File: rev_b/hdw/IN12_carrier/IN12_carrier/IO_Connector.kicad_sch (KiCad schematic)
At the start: 0 parts

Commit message: lots of placement progress on IN12 carrier board
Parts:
- added J1901: Conn_02x32_Top_Bottom, Custom Footprints Library:CONN_5120528-1_TYC, symbol Connector_Generic:Conn_02x32_Top_Bottom
- added R?: 499, Resistors_SMD:R_0603, symbol Custom_Library:R_Custom
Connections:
- new net +180V: J1901.36 (Pin_36), J1901.37 (Pin_37)
- new net +3.3V: J1901.61 (Pin_61), J1901.62 (Pin_62), J1901.63 (Pin_63), J1901.64 (Pin_64)
- new net +90V: J1901.33 (Pin_33), J1901.34 (Pin_34)
- new net Anode_0_DSP: J1901.39 (Pin_39)
- new net Anode_1_DSP: J1901.7 (Pin_7)
- new net Anode_2_DSP: J1901.40 (Pin_40)
- new net Anode_3_DSP: J1901.8 (Pin_8)
- new net Anode_4_DSP: J1901.41 (Pin_41)
- new net Anode_5_DSP: J1901.9 (Pin_9)
- new net Cathode_0_DSP: J1901.43 (Pin_43)
- new net Cathode_1_DSP: J1901.11 (Pin_11)
- new net Cathode_2_DSP: J1901.44 (Pin_44)
- new net Cathode_3_DSP: J1901.12 (Pin_12)
- new net Cathode_4_DSP: J1901.45 (Pin_45)
- new net Cathode_5_DSP: J1901.13 (Pin_13)
- new net Cathode_6_DSP: J1901.46 (Pin_46)
- new net Cathode_7_DSP: J1901.14 (Pin_14)
- new net Cathode_8_DSP: J1901.47 (Pin_47)
- new net Cathode_9_DSP: J1901.15 (Pin_15)
- new net Cathode_DP_DSP: J1901.48 (Pin_48)
- new net Colon_0_DSP: J1901.50 (Pin_50)
- new net Colon_1_DSP: J1901.18 (Pin_18)
- new net Colon_2_DSP: J1901.51 (Pin_51)
- new net Colon_3_DSP: J1901.19 (Pin_19)
- new net GND: J1901.1 (Pin_1), J1901.10 (Pin_10), J1901.16 (Pin_16), J1901.17 (Pin_17), J1901.2 (Pin_2), J1901.20 (Pin_20), J1901.24 (Pin_24), J1901.25 (Pin_25), J1901.29 (Pin_29), J1901.3 (Pin_3), J1901.30 (Pin_30), J1901.31 (Pin_31), J1901.32 (Pin_32), J1901.4 (Pin_4), J1901.42 (Pin_42), J1901.49 (Pin_49), J1901.5 (Pin_5), J1901.52 (Pin_52), J1901.6 (Pin_6), R?.2
- new net I2C_DSP_SCL: J1901.58 (Pin_58)
- new net I2C_DSP_SDA: J1901.26 (Pin_26)
- new net Pushbutton_0_DSP: J1901.53 (Pin_53)
- new net Pushbutton_1_DSP: J1901.21 (Pin_21)
- new net Pushbutton_2_DSP: J1901.54 (Pin_54)
- new net Pushbutton_3_DSP: J1901.22 (Pin_22)
- new net Pushbutton_4_DSP: J1901.55 (Pin_55)
- new net Pushbutton_5_DSP: J1901.23 (Pin_23)
- new net Pushbutton_6_DSP: J1901.56 (Pin_56)
- new net USB_UART_RX: J1901.27 (Pin_27)
- new net USB_UART_TX: J1901.59 (Pin_59)
- new net ~{Display_Detect_DSP}: J1901.57 (Pin_57), R?.1
- no-connect marks 0 -> 4

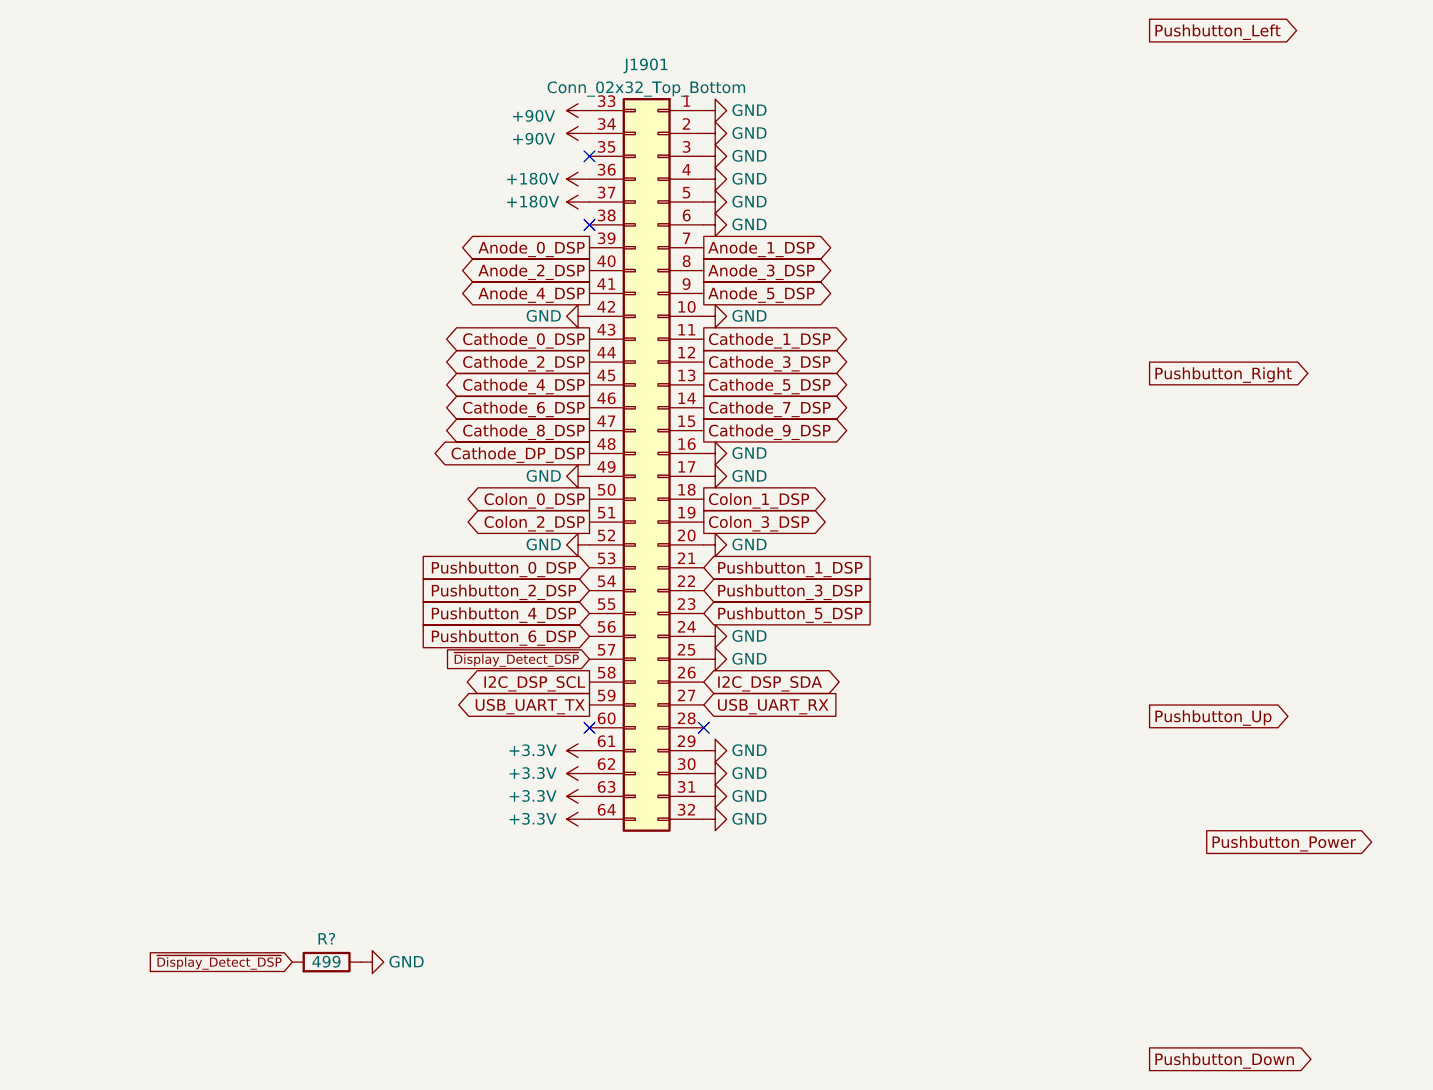
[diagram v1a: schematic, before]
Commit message: lots of routing and design progress on IN12 carrier board
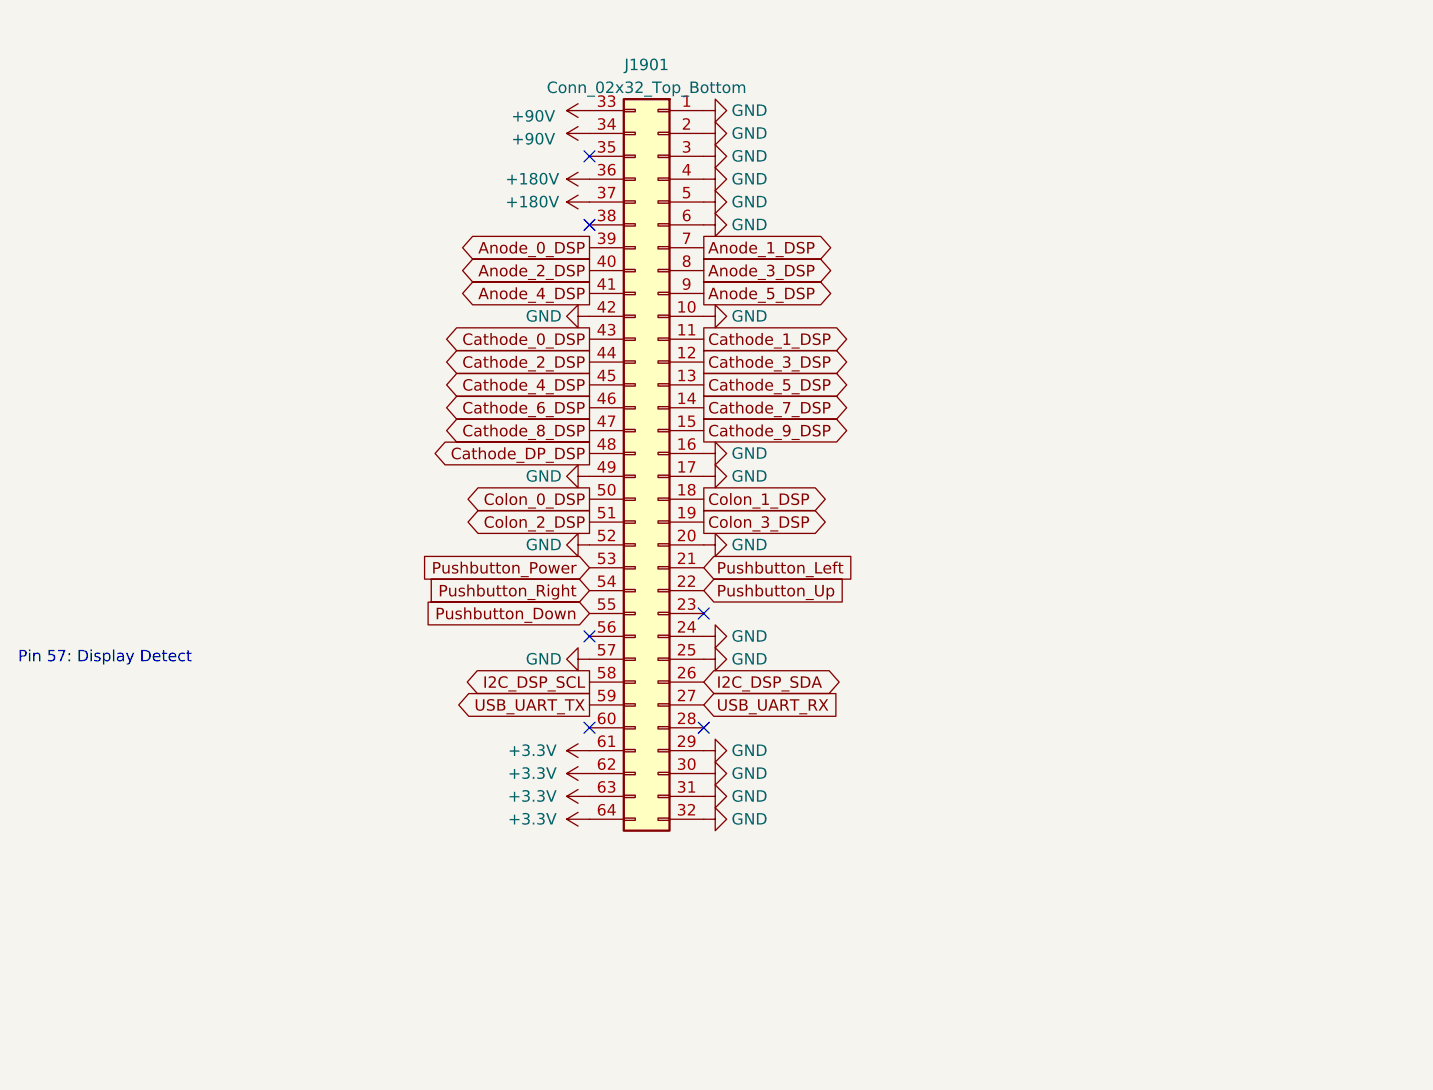
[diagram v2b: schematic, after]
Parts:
- removed R?: 499, Resistors_SMD:R_0603, symbol Custom_Library:R_Custom
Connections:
- net Pushbutton_0_DSP is gone; now on net Pushbutton_Power: J1901.53 (Pin_53)
- net Pushbutton_1_DSP is gone; now on net Pushbutton_Left: J1901.21 (Pin_21)
- net Pushbutton_2_DSP is gone; now on net Pushbutton_Right: J1901.54 (Pin_54)
- net Pushbutton_3_DSP is gone; now on net Pushbutton_Up: J1901.22 (Pin_22)
- net Pushbutton_4_DSP is gone; now on net Pushbutton_Down: J1901.55 (Pin_55)
- net ~{Display_Detect_DSP} is gone; now on net GND: J1901.57 (Pin_57)
- net Pushbutton_5_DSP: no longer names the net of J1901.23 (Pin_23)
- net Pushbutton_6_DSP: no longer names the net of J1901.56 (Pin_56)
- no-connect marks 4 -> 6
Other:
- note added: "Pin 57: Display Detect"
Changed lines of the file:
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@@
   (no_connect (at 114.935 55.245))
   (no_connect (at 114.935 62.865))
+  (no_connect (at 114.935 108.585))
+  (no_connect (at 127.635 106.045))
   (no_connect (at 127.635 118.745))
-  (global_label "~{Display_Detect_DSP}" (shape input) (at 81.915 144.78 180)
-    (effects (font (size 1.016 1.016)) (justify right))
-    (property "Intersheetrefs" "${INTERSHEET_REFS}" (at 81.915 144.78 0)
-      (effects (font (size 1.27 1.27)) hide)
-    )
+  (text "Pin 57: Display Detect" (at 51.435 111.76 0)
+    (effects (font (size 1.27 1.27)) (justify left bottom))
   )
   (global_label "USB_UART_RX" (shape input) (at 127.635 116.205 0)
@@
     )
   )
-  (global_label "Pushbutton_Power" (shape output) (at 183.515 131.445 0)
-    (effects (font (size 1.27 1.27)) (justify left))
-    (property "Intersheetrefs" "${INTERSHEET_REFS}" (at 183.515 131.445 0)
+  (global_label "Pushbutton_Power" (shape input) (at 114.935 100.965 180)
+    (effects (font (size 1.27 1.27)) (justify right))
+    (property "Intersheetrefs" "${INTERSHEET_REFS}" (at 114.935 100.965 0)
       (effects (font (size 1.27 1.27)) hide)
     )
@@
     )
   )
-  (global_label "Pushbutton_3_DSP" (shape input) (at 127.635 103.505 0) (fields_autoplaced)
-    (effects (font (size 1.27 1.27)) (justify left))
-    (property "Intersheetrefs" "${INTERSHEET_REFS}" (at 148.0785 103.505 0)
-      (effects (font (size 1.27 1.27)) (justify left) hide)
-    )
-  )
   (global_label "I2C_DSP_SDA" (shape bidirectional) (at 127.635 113.665 0)
     (effects (font (size 1.27 1.27)) (justify left))
@@
     )
   )
-  (global_label "Pushbutton_Up" (shape output) (at 177.165 117.475 0)
-    (effects (font (size 1.27 1.27)) (justify left))
-    (property "Intersheetrefs" "${INTERSHEET_REFS}" (at 177.165 117.475 0)
+  (global_label "Pushbutton_Up" (shape input) (at 127.635 103.505 0)
+    (effects (font (size 1.27 1.27)) (justify left))
+    (property "Intersheetrefs" "${INTERSHEET_REFS}" (at 127.635 103.505 0)
       (effects (font (size 1.27 1.27)) hide)
     )
@@
     )
   )
-  (global_label "~{Display_Detect_DSP}" (shape input) (at 114.935 111.125 180)
-    (effects (font (size 1.016 1.016)) (justify right))
-    (property "Intersheetrefs" "${INTERSHEET_REFS}" (at 114.935 111.125 0)
-      (effects (font (size 1.27 1.27)) hide)
-    )
-  )
-  (global_label "Pushbutton_Left" (shape output) (at 177.165 41.275 0)
-    (effects (font (size 1.27 1.27)) (justify left))
-    (property "Intersheetrefs" "${INTERSHEET_REFS}" (at 177.165 41.275 0)
+  (global_label "Pushbutton_Left" (shape input) (at 127.635 100.965 0)
+    (effects (font (size 1.27 1.27)) (justify left))
+    (property "Intersheetrefs" "${INTERSHEET_REFS}" (at 127.635 100.965 0)
       (effects (font (size 1.27 1.27)) hide)
     )
@@
     )
   )
-  (global_label "Pushbutton_Right" (shape output) (at 177.165 79.375 0)
-    (effects (font (size 1.27 1.27)) (justify left))
-    (property "Intersheetrefs" "${INTERSHEET_REFS}" (at 177.165 79.375 0)
+  (global_label "Pushbutton_Right" (shape input) (at 114.935 103.505 180)
+    (effects (font (size 1.27 1.27)) (justify right))
+    (property "Intersheetrefs" "${INTERSHEET_REFS}" (at 114.935 103.505 0)
       (effects (font (size 1.27 1.27)) hide)
     )
@@
     )
   )
-  (global_label "Pushbutton_Down" (shape output) (at 177.165 155.575 0)
-    (effects (font (size 1.27 1.27)) (justify left))
-    (property "Intersheetrefs" "${INTERSHEET_REFS}" (at 177.165 155.575 0)
+  (global_label "Pushbutton_Down" (shape input) (at 114.935 106.045 180)
+    (effects (font (size 1.27 1.27)) (justify right))
+    (property "Intersheetrefs" "${INTERSHEET_REFS}" (at 114.935 106.045 0)
       (effects (font (size 1.27 1.27)) hide)
     )
@@
     )
   )
-  (global_label "Pushbutton_0_DSP" (shape input) (at 114.935 100.965 180) (fields_autoplaced)
-    (effects (font (size 1.27 1.27)) (justify right))
-    (property "Intersheetrefs" "${INTERSHEET_REFS}" (at 94.4915 100.965 0)
-      (effects (font (size 1.27 1.27)) (justify right) hide)
-    )
-  )
   (global_label "Colon_3_DSP" (shape output) (at 127.635 95.885 0) (fields_autoplaced)
     (effects (font (size 1.27 1.27)) (justify left))
@@
     )
   )
-  (global_label "Pushbutton_2_DSP" (shape input) (at 114.935 103.505 180) (fields_autoplaced)
-    (effects (font (size 1.27 1.27)) (justify right))
-    (property "Intersheetrefs" "${INTERSHEET_REFS}" (at 94.4915 103.505 0)
-      (effects (font (size 1.27 1.27)) (justify right) hide)
-    )
-  )
   (global_label "Cathode_6_DSP" (shape output) (at 114.935 83.185 180) (fields_autoplaced)
     (effects (font (size 1.27 1.27)) (justify right))
@@
     )
   )
-  (global_label "Pushbutton_5_DSP" (shape input) (at 127.635 106.045 0) (fields_autoplaced)
-    (effects (font (size 1.27 1.27)) (justify left))
-    (property "Intersheetrefs" "${INTERSHEET_REFS}" (at 148.0785 106.045 0)
-      (effects (font (size 1.27 1.27)) (justify left) hide)
-    )
-  )
   (global_label "Colon_1_DSP" (shape output) (at 127.635 93.345 0) (fields_autoplaced)
     (effects (font (size 1.27 1.27)) (justify left))
@@
     (property "Intersheetrefs" "${INTERSHEET_REFS}" (at 145.1153 78.105 0)
       (effects (font (size 1.27 1.27)) (justify left) hide)
-    )
-  )
-  (global_label "Pushbutton_4_DSP" (shape input) (at 114.935 106.045 180) (fields_autoplaced)
-    (effects (font (size 1.27 1.27)) (justify right))
-    (property "Intersheetrefs" "${INTERSHEET_REFS}" (at 94.4915 106.045 0)
-      (effects (font (size 1.27 1.27)) (justify right) hide)
-    )
-  )
-  (global_label "Pushbutton_1_DSP" (shape input) (at 127.635 100.965 0) (fields_autoplaced)
-    (effects (font (size 1.27 1.27)) (justify left))
-    (property "Intersheetrefs" "${INTERSHEET_REFS}" (at 148.0785 100.965 0)
-      (effects (font (size 1.27 1.27)) (justify left) hide)
-    )
-  )
-  (global_label "Pushbutton_6_DSP" (shape input) (at 114.935 108.585 180) (fields_autoplaced)
-    (effects (font (size 1.27 1.27)) (justify right))
-    (property "Intersheetrefs" "${INTERSHEET_REFS}" (at 94.4915 108.585 0)
-      (effects (font (size 1.27 1.27)) (justify right) hide)
     )
   )
@@
     )
   )
-  (symbol (lib_id "power:GND") (at 89.535 144.78 90) (mirror x) (unit 1)
-    (in_bom yes) (on_board yes) (dnp no)
-    (property "Reference" "#PWR01910" (at 95.885 144.78 0)
-      (effects (font (size 1.27 1.27)) hide)
-    )
-    (property "Value" "GND" (at 94.615 144.78 90)
-      (effects (font (size 1.27 1.27)))
-    )
-    (property "Footprint" "" (at 89.535 144.78 0)
-      (effects (font (size 1.27 1.27)) hide)
-    )
-    (property "Datasheet" "" (at 89.535 144.78 0)
+  (symbol (lib_id "power:GND") (at 114.935 111.125 270) (mirror x) (unit 1)
+    (in_bom yes) (on_board yes) (dnp no)
+    (property "Reference" "#PWR01910" (at 108.585 111.125 0)
+      (effects (font (size 1.27 1.27)) hide)
+    )
+    (property "Value" "GND" (at 109.855 111.125 90)
+      (effects (font (size 1.27 1.27)))
+    )
+    (property "Footprint" "" (at 114.935 111.125 0)
+      (effects (font (size 1.27 1.27)) hide)
+    )
+    (property "Datasheet" "" (at 114.935 111.125 0)
       (effects (font (size 1.27 1.27)) hide)
     )
@@
         )
       )
-    )
-  )
-  (symbol (lib_id "Custom_Library:R_Custom") (at 85.725 144.78 90) (mirror x) (unit 1)
-    (in_bom yes) (on_board yes) (dnp no)
-    (property "Reference" "R?" (at 85.725 142.24 90)
-      (effects (font (size 1.27 1.27)))
-    )
-    (property "Value" "499" (at 85.725 144.78 90)
-      (effects (font (size 1.27 1.27)))
-    )
-    (property "Footprint" "Resistors_SMD:R_0603" (at 85.725 144.78 0)
-      (effects (font (size 1.27 1.27)) hide)
-    )
-    (property "Datasheet" "" (at 85.725 144.78 0)
-      (effects (font (size 1.27 1.27)) hide)
-    )
-    (property "Digi-Key PN" "" (at 75.565 152.4 0)
-      (effects (font (size 1.524 1.524)) hide)
-    )
-    (property "display_footprint" "0603" (at 85.725 147.32 90)
-      (effects (font (size 1.27 1.27)) hide)
-    )
-    (property "Tolerance" "1%" (at 85.725 149.86 90)
-      (effects (font (size 1.27 1.27)) hide)
-    )
-    (property "Wattage" "1/10W" (at 85.725 152.4 90)
-      (effects (font (size 1.27 1.27)) hide)
-    )
-    (pin "1")
-    (pin "2")
-    (instances
-      (project "IV-6_Display_Board"
-        (path "/1e596753-9bad-4a10-9dfd-a62cc0cd3802/00000000-0000-0000-0000-00005c26e09a"
-          (reference "R?") (unit 1)
-        )
-        (path "/1e596753-9bad-4a10-9dfd-a62cc0cd3802/00000000-0000-0000-0000-00005e28cfdf"
-          (reference "R?") (unit 1)
-        )
-        (path "/1e596753-9bad-4a10-9dfd-a62cc0cd3802/00000000-0000-0000-0000-00005e3c80c8"
-          (reference "R?") (unit 1)
-        )
-        (path "/1e596753-9bad-4a10-9dfd-a62cc0cd3802/00000000-0000-0000-0000-00005e3cbfda"
-          (reference "R?") (unit 1)
-        )
-        (path "/1e596753-9bad-4a10-9dfd-a62cc0cd3802/00000000-0000-0000-0000-00005c3165d8"
-          (reference "R?") (unit 1)
-        )
-        (path "/1e596753-9bad-4a10-9dfd-a62cc0cd3802/00000000-0000-0000-0000-00005e36ce18"
-          (reference "R?") (unit 1)
-        )
-        (path "/1e596753-9bad-4a10-9dfd-a62cc0cd3802/00000000-0000-0000-0000-00005e0a7959"
-          (reference "R511") (unit 1)
-        )
-        (path "/1e596753-9bad-4a10-9dfd-a62cc0cd3802/00000000-0000-0000-0000-00005e3c97b4"
-          (reference "R?") (unit 1)
-        )
-        (path "/1e596753-9bad-4a10-9dfd-a62cc0cd3802/00000000-0000-0000-0000-00005d739492"
-          (reference "R?") (unit 1)
-        )
-      )
-      (project "IN12_carrier"
-        (path "/c4d83a5b-e6ae-4326-9df5-0c4ac01f7d8c/815dbf76-232e-4bad-8c07-aee05ae43ace"
-          (reference "R1011") (unit 1)
-        )
-        (path "/c4d83a5b-e6ae-4326-9df5-0c4ac01f7d8c/69adbe3d-b414-4221-86a2-c186a7447efb"
-          (reference "R201") (unit 1)
-        )
-      )

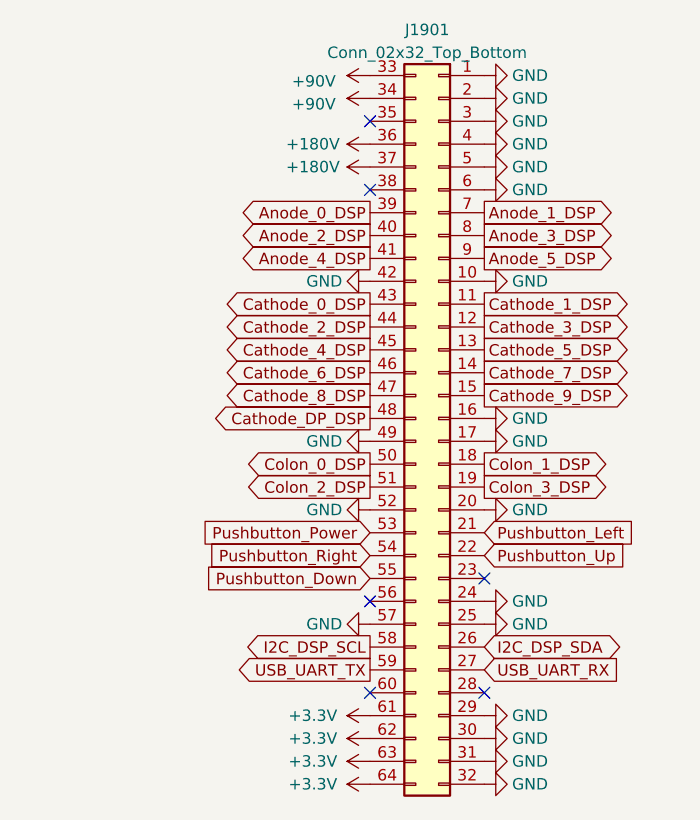
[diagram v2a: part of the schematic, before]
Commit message: got IN12 carrier board unconnects to 0
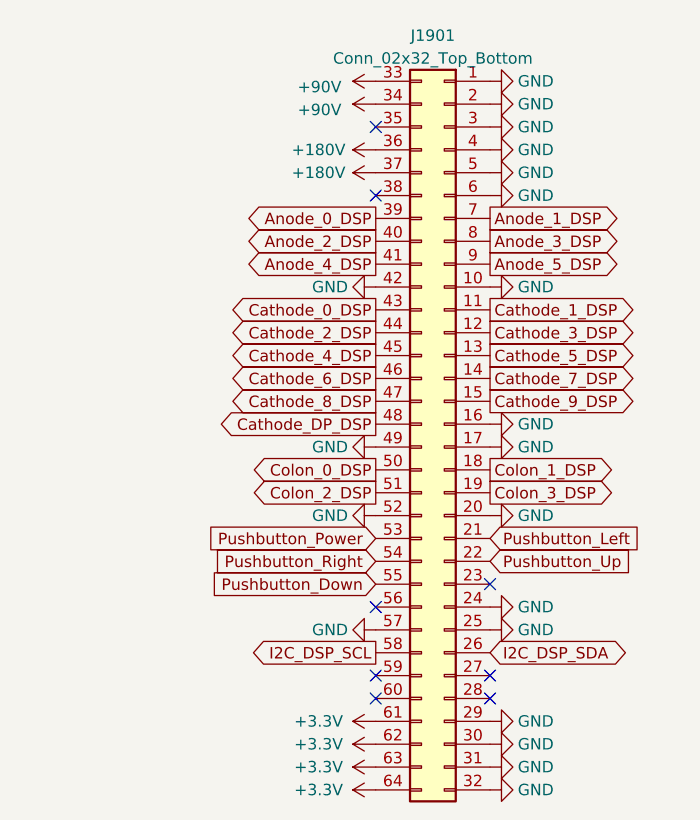
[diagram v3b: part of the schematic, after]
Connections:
- net USB_UART_RX: no longer names the net of J1901.27 (Pin_27)
- net USB_UART_TX: no longer names the net of J1901.59 (Pin_59)
- no-connect marks 6 -> 8
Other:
- moved on the sheet: J1901

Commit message: added BOM for IN12 carrier, finished routing, some schematic tweaks, adjusted design rules for ERC
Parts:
- J1901: Digi-Key PN A111226CT-ND -> A104089CT-ND
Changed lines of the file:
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@@
       (effects (font (size 1.27 1.27)) hide)
     )
-    (property "Digi-Key PN" "A111226CT-ND" (at 123.19 88.9 0)
+    (property "Digi-Key PN" "A104089CT-ND" (at 123.19 88.9 0)
       (effects (font (size 1.27 1.27)) hide)
     )
